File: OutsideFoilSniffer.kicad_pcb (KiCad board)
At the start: 2 copper layers, 79.5 x 99.5 mm, 40 parts, among them J1 Black, J2 Red, J3 Signal, J4 Conn_01x15_Male, J5 Conn_01x15_Male, K1 SANYOU_SRD_Form_C, Q1 BC547, Q2 2N3904

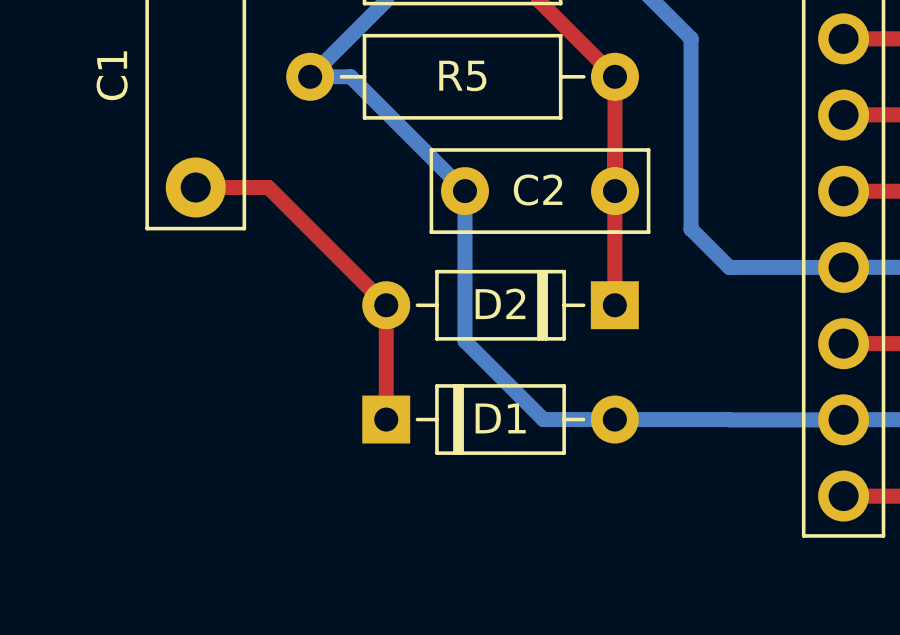
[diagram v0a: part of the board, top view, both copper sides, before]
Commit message: Added sniffer code modified for my design. Code needs serious cleanup
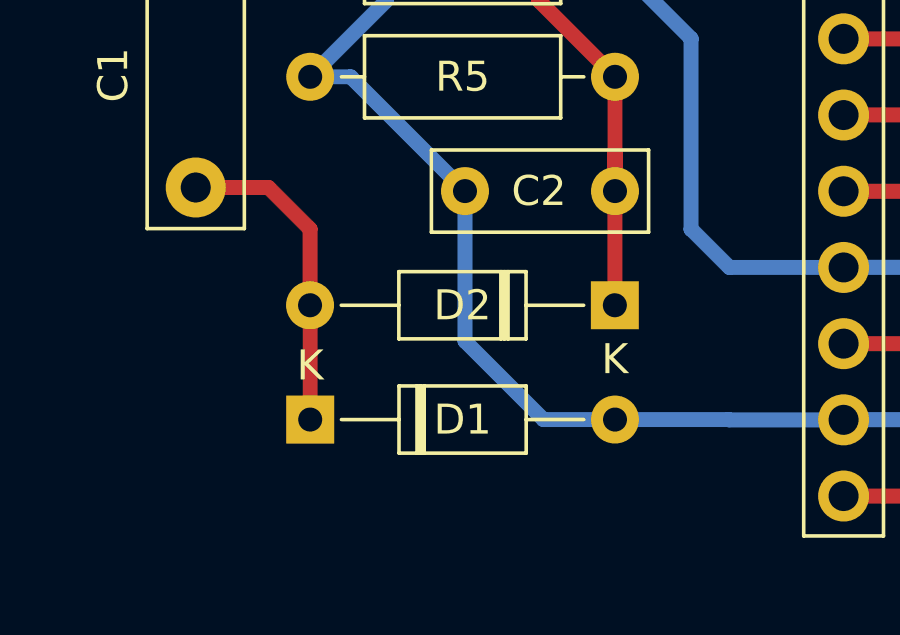
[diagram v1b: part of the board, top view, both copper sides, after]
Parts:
- D1, D2: footprint Diode_THT:D_DO-35_SOD27_P7.62mm_Horizontal -> Diode_THT:D_DO-35_SOD27_P10.16mm_Horizontal
- R1: value R -> 470K
- R10, R9: value R -> 220
- R2: value R -> 4K7
- R3: value R -> 1K
- R4, R8: value R -> 10K
- R5: value R -> 100K
- R6, R7: value R -> 470
- moved D1 2.53 mm to (68.6, 99.1)
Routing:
- net Net-(C1-Pad1): track 11.8 -> 10.7 mm

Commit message: minor changes
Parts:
- Q1, Q2: footprint Package_TO_SOT_THT:TO-92_Inline -> Package_TO_SOT_THT:TO-92_Inline_Wide
- moved D5 3.18 mm to (61.0, 142.9)
- moved D6 3.18 mm to (128.3, 142.9)
- moved R10 3.18 mm to (61.0, 135.3)
- moved R9 3.18 mm to (128.3, 125.1)
- moved JP5 3.17 mm to (61.0, 120.0)
- moved JP6 3.17 mm to (128.3, 120.0)
- moved Q2 1.91 mm to (91.7, 118.7)
- moved D3 0.30 mm to (99.1, 132.1)
- moved R4 0.30 mm to (88.9, 128.3)
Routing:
- net PINGND: track 237.6 -> 141.9 mm
- net PIN9: track 58.4 -> 55.2 mm
- net PIN8: track 73.5 -> 72.2 mm
- net Net-(Q2-Pad2): track 12.5 -> 13.2 mm
